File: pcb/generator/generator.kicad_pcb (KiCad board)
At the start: 2 copper layers, 77.5 x 104.5 mm, 53 parts, among them J1 Power, J2 SWD, J3 CH1, J4 CH2, J5 USB, U1 ATSAMD11D14A-SS, U2 SRH05S3V3, U3 L6206D, U4 MCP9700T-HLT, U5 LP2985-3.3, U6 SN65220, Y1 32.768kHz

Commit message: Release preparation
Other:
- board text added: "Meadow Robotics GmbH"
- board text added: "Perimeter Wire Generator R1"
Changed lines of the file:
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@@
   (general
     (thickness 1.6)
-    (drawings 17)
+    (drawings 19)
     (tracks 1861)
     (zones 0)
@@
   )
   (page A4)
+  (title_block
+    (title "Permimeter Wire Generator")
+    (date 2019-09-02)
+    (rev R1)
+    (company "Meadow Robotics GmbH")
+  )
   (layers
     (0 F.Cu signal)
@@
     )
   )
+  (gr_text "Perimeter Wire Generator\nR1" (at 50.8 67.945) (layer F.SilkS)
+    (effects (font (size 1 1) (thickness 0.15)) (justify left))
+  )
+  (gr_text "Meadow Robotics GmbH" (at 50.8 65.405) (layer F.SilkS)
+    (effects (font (size 1 1) (thickness 0.15)) (justify left))
+  )
   (gr_text "USB\n" (at 66.675 58.42) (layer F.SilkS)

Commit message: generator: pcb for modulbox
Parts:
- removed D2: D, Diode_THT:D_DO-35_SOD27_P7.62mm_Horizontal
- removed H1, H2, H3: MountingHole_Pad, MountingHole:MountingHole_3.2mm_M3_Pad
- added C19: 100n, Capacitor_SMD:C_0805_2012Metric, F.Cu at (155.6, 78.1)
- added C9: 100n, Capacitor_SMD:C_0805_2012Metric, F.Cu at (156.2, 57.8)
- added D8: 48V, Diode_SMD:D_SMB, F.Cu at (54.0, 87.6)
- added E1: SPARK_GAP, footprints:Spark_Gap_0.4_Pwr, B.Cu at (43.2, 84.7)
- added E2: SPARK_GAP, footprints:Spark_Gap_0.4_Pwr, B.Cu at (40.6, 47.0)
- added E3: SPARK_GAP, footprints:Spark_Gap_0.4_Pwr, B.Cu at (40.6, 52.1)
- added E4: SPARK_GAP, footprints:Spark_Gap_0.4_Pwr, B.Cu at (40.6, 57.1)
- added E5: SPARK_GAP, footprints:Spark_Gap_0.4_Pwr, B.Cu at (40.6, 62.2)
- added E6: SPARK_GAP, footprints:Spark_Gap_0.4_Pwr, B.Cu at (40.6, 67.3)
- added E7: SPARK_GAP, footprints:Spark_Gap_0.4_Pwr, B.Cu at (40.6, 71.8)
- added FID3: Fiducial, Fiducial:Fiducial_1mm_Mask2mm, F.Cu at (160.0, 84.5)
- added FID4: Fiducial, Fiducial:Fiducial_1mm_Mask2mm, F.Cu at (141.6, 62.2)
- added FID5: Fiducial, Fiducial:Fiducial_1mm_Mask2mm, F.Cu at (130.2, 45.7)
- added FID6: Fiducial, Fiducial:Fiducial_1mm_Mask2mm, F.Cu at (84.5, 54.0)
- added J6: Au, Connector_PinSocket_2.54mm:PinSocket_2x05_P2.54mm_Vertical, B.Cu at (147.2, 47.6)
- added J7: Bu, Connector_PinSocket_2.54mm:PinSocket_2x05_P2.54mm_Vertical, B.Cu at (157.3, 86.4)
- added J8: Al, Connector_PinHeader_2.54mm:PinHeader_2x05_P2.54mm_Vertical, F.Cu at (80.6, 47.6)
- added J9: Bl, Connector_PinHeader_2.54mm:PinHeader_2x05_P2.54mm_Vertical, F.Cu at (90.8, 85.7)
- added R11: 280R, Resistor_SMD:R_0805_2012Metric, F.Cu at (138.4, 53.3)
- added R12: 280R, Resistor_SMD:R_0805_2012Metric, F.Cu at (138.4, 61.0)
- added R13: 100R, Resistor_SMD:R_0805_2012Metric, F.Cu at (138.4, 48.3)
- added R14: 100R, Resistor_SMD:R_0805_2012Metric, F.Cu at (138.4, 50.8)
- added R15: 100R, Resistor_SMD:R_0805_2012Metric, F.Cu at (138.4, 58.4)
- added R16: 100R, Resistor_SMD:R_0805_2012Metric, F.Cu at (138.4, 55.9)
- added R17: 100R, Resistor_SMD:R_0805_2012Metric, F.Cu at (109.2, 46.4)
- C10, C11, C12, C13, C8: footprint Capacitor_THT:C_Disc_D5.1mm_W3.2mm_P5.00mm -> Capacitor_SMD:C_0805_2012Metric
- C14, C15: value 20p -> 22p; footprint Capacitor_THT:C_Disc_D3.8mm_W2.6mm_P2.50mm -> Capacitor_SMD:C_0805_2012Metric
- C16, C17, C3, C4, C5, C6, C7: footprint Capacitor_THT:C_Disc_D4.7mm_W2.5mm_P5.00mm -> Capacitor_SMD:C_0805_2012Metric
- C18: footprint Capacitor_THT:CP_Radial_D5.0mm_P2.00mm -> Capacitor_Tantalum_SMD:CP_EIA-6032-28_Kemet-C
- D1: footprint Diode_THT:D_DO-35_SOD27_P7.62mm_Horizontal -> Package_TO_SOT_SMD:SOT-23
- D3: value Red1 -> CLMVC-FKA; footprint LED_THT:LED_D5.0mm -> LED_SMD:LED_Cree-PLCC4_2x2mm_CW
- D4: value Red2 -> CLMVC-FKA; footprint LED_THT:LED_D5.0mm -> LED_SMD:LED_Cree-PLCC4_2x2mm_CW
- D5: footprint Diode_THT:D_DO-15_P10.16mm_Horizontal -> Diode_SMD:D_SMB
- FB1: value BLM31KN471SN1L -> BLM31KN471SN1L
- FB2: value BLM31SN500SN1 -> BLM31SN500SN1L
- FID1, FID2: footprint Fiducial:Fiducial_1.5mm_Mask3mm -> Fiducial:Fiducial_1mm_Mask2mm
- J1: footprint Connector_Phoenix_MSTB:PhoenixContact_MSTBA_2,5_2-G_1x02_P5.00mm_Horizontal -> TerminalBlock:TerminalBlock_bornier-2_P5.08mm
- J2: footprint Connector_PinHeader_1.27mm:PinHeader_2x05_P1.27mm_Vertical -> Connector_PinHeader_1.27mm:PinHeader_2x05_P1.27mm_Vertical_SMD
- J3, J4: footprint Connector_Phoenix_MSTB:PhoenixContact_MSTBA_2,5_3-G-5,08_1x03_P5.08mm_Horizontal -> TerminalBlock:TerminalBlock_bornier-3_P5.08mm
- J5: footprint Connector_USB:USB_Micro-B_Amphenol_10103594-0001LF_Horizontal -> Connector_USB:USB_Micro-B_Molex-105133-0001
- R1, R2: value 10k -> 22k; footprint Resistor_THT:R_Axial_DIN0207_L6.3mm_D2.5mm_P7.62mm_Horizontal -> Resistor_SMD:R_0805_2012Metric
- R10, R4, R5: footprint Resistor_THT:R_Axial_DIN0207_L6.3mm_D2.5mm_P7.62mm_Horizontal -> Resistor_SMD:R_0805_2012Metric
- R3: value 100 -> 22k; footprint Resistor_THT:R_Axial_DIN0207_L6.3mm_D2.5mm_P7.62mm_Horizontal -> Resistor_SMD:R_0805_2012Metric
- R6, R7: value 240 -> 200R; footprint Resistor_THT:R_Axial_Power_L48.0mm_W12.5mm_P60.96mm -> footprints:Ohmite-TKH
- R8: value 750R -> 1k; footprint Resistor_THT:R_Axial_DIN0207_L6.3mm_D2.5mm_P7.62mm_Horizontal -> Resistor_SMD:R_0805_2012Metric
- R9: value 750R -> 1M; footprint Resistor_THT:R_Axial_DIN0207_L6.3mm_D2.5mm_P7.62mm_Horizontal -> Resistor_SMD:R_0805_2012Metric
- U1: value ATSAMD11D14A-SS -> ATSAMD21E; footprint Package_SO:SOIC-20W_7.5x12.8mm_P1.27mm -> Package_QFP:TQFP-32_7x7mm_P0.8mm
- U3: value L6206D -> L6206
- Y1: value 32.768kHz -> 16MHz; footprint Crystal:Crystal_SMD_SeikoEpson_MC146-4Pin_6.7x1.5mm_HandSoldering -> Crystal:Crystal_SMD_SeikoEpson_TSX3225-4Pin_3.2x2.5mm
- moved J1 104.4 mm to (43.2, 82.2), turned to 270 degrees
- moved R1 100.2 mm to (155.6, 54.0), turned to 270 degrees
- moved R2 100.1 mm to (155.6, 80.6), turned to 0 degrees
- moved FB2 85.4 mm to (57.9, 87.4), turned to 90 degrees
- moved R3 79.9 mm to (164.5, 64.8), turned to 0 degrees
- moved C12 78.6 mm to (60.3, 87.6)
- moved J4 76.4 mm to (43.2, 61.9)
- moved C17 75.7 mm to (130.2, 60.3)
- moved C8 75.5 mm to (117.3, 46.4)
- moved C11 74.6 mm to (97.2, 75.6), turned to 180 degrees
- moved R5 74.5 mm to (90.2, 78.1)
- moved C1 74.3 mm to (96.5, 47.6), turned to 0 degrees
- moved C3 72.1 mm to (153.7, 70.5), turned to 0 degrees
- moved J3 71.7 mm to (43.2, 46.6)
- moved J5 71.1 mm to (135.9, 66.7), turned to 270 degrees
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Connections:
- D1 pad 1: Net-(D1-Pad1) -> +48V
- D1 pad 2: +48V -> Net-(C8-Pad1)
- D3 pad 1: Net-(D3-Pad1) -> +3V3
- D3 pad 2: +3V3 -> Net-(D3-Pad2)
- D4 pad 1: Net-(D4-Pad1) -> +3V3
- D4 pad 2: +3V3 -> Net-(D4-Pad2)
- J3 pad 2: Net-(J3-Pad2) -> Net-(E3-Pad1)
- J3 pad 3: Net-(J3-Pad3) -> Net-(E4-Pad1)
- J4 pad 2: Net-(J4-Pad2) -> Net-(E6-Pad1)
- J4 pad 3: Net-(J4-Pad3) -> Net-(E7-Pad1)
- R3 pad 1: Net-(C16-Pad2) -> /V_SENSE
- R3 pad 2: Net-(D1-Pad1) -> GND
- R6 pad 1: Net-(J3-Pad3) -> Net-(E3-Pad1)
- R6 pad 2: Net-(J3-Pad2) -> GND
- R7 pad 1: Net-(J4-Pad3) -> Net-(E6-Pad1)
- R7 pad 2: Net-(J4-Pad2) -> GND
- R8 pad 1: Net-(D3-Pad1) -> +3V3
- R8 pad 2: Net-(R8-Pad2) -> /SWCLK
- R9 pad 1: Net-(D4-Pad1) -> +48V
- R9 pad 2: Net-(R9-Pad2) -> /V_SENSE
- U1 pad 1: /IN2_B -> /EN_B
- U1 pad 10: Net-(R9-Pad2) -> GND
- U1 pad 11: /~RESET -> /EN_A
- U1 pad 12: /SWCLK -> /ERROR_A
- U1 pad 13: /SWDIO -> (no net)
- U1 pad 14: /USB_D- -> (no net)
- U1 pad 15: /USB_D+ -> Net-(C14-Pad1)
- U1 pad 16: GND -> Net-(C15-Pad2)
- U1 pad 17: +3V3 -> Net-(R13-Pad2)
- U1 pad 18: /EN_B -> Net-(R14-Pad2)
- U1 pad 19: /ERROR_B -> Net-(R11-Pad2)
- U1 pad 2: /IN1_A -> /ERROR_B
- U1 pad 20: /IN1_B -> Net-(R16-Pad2)
- U1 pad 3: /IN2_A -> /IN1_B
- U1 pad 4: Net-(C14-Pad1) -> /IN2_B
- U1 pad 5: Net-(C15-Pad2) -> /V_SENSE
- U1 pad 6: /EN_A -> /R_TEMP
- U1 pad 7: /ERROR_A -> /IN1_A
- U1 pad 8: /R_TEMP -> /IN2_A
- U1 pad 9: Net-(R8-Pad2) -> +3V3
- U3 pad 15: Net-(J3-Pad2) -> Net-(E3-Pad1)
- U3 pad 22: Net-(J4-Pad2) -> Net-(E6-Pad1)
- Y1 pad 3: GND -> Net-(C15-Pad2)
- Y1 pad 4: Net-(C15-Pad2) -> GND
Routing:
- net GND: track 641.8 -> 162.0 mm, vias 1102 -> 434
- net /EN_B: track 170.1 -> 15.8 mm
- net /ERROR_B: track 186.5 -> 59.4 mm, vias 2 -> 1
- net /IN1_B: track 167.1 -> 43.3 mm, vias 4 -> 1
- net /IN2_B: track 152.7 -> 41.7 mm, vias 4 -> 1
- net Net-(J3-Pad3): track 110.0 -> 0.00 mm, vias 2 -> 0
- net Net-(J4-Pad3): track 108.4 -> 0.00 mm
- net /EN_A: track 101.1 -> 5.53 mm, vias 2 -> 0
- net /ERROR_A: track 120.1 -> 37.8 mm, vias 4 -> 2
- net Net-(J4-Pad2): track 80.6 -> 0.00 mm
- net Net-(J3-Pad2): track 78.6 -> 0.00 mm
- net /IN1_A: track 108.2 -> 37.2 mm, vias 4 -> 1
- net +48V: track 151.8 -> 222.7 mm, vias 1 -> 0
- net (no net): track 70.3 -> 0.00 mm, vias 4 -> 0
- net /IN2_A: track 107.6 -> 37.7 mm, vias 4 -> 1
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- added copper zone on F.Cu, net +3V3
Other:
- board size 77.5 x 104.5 mm -> 131 x 50.2 mm
- net class Default: clearance 0.2 -> 0.19
- rule trace_clearance: 0.2 -> 0.19
- board text added: "Meadow Robotics GmbH Perimeter Wire Generator R2"
- board text removed: "Meadow Robotics GmbH"
- board text removed: "Perimeter Wire Generator R1"
- board text removed: "USB"

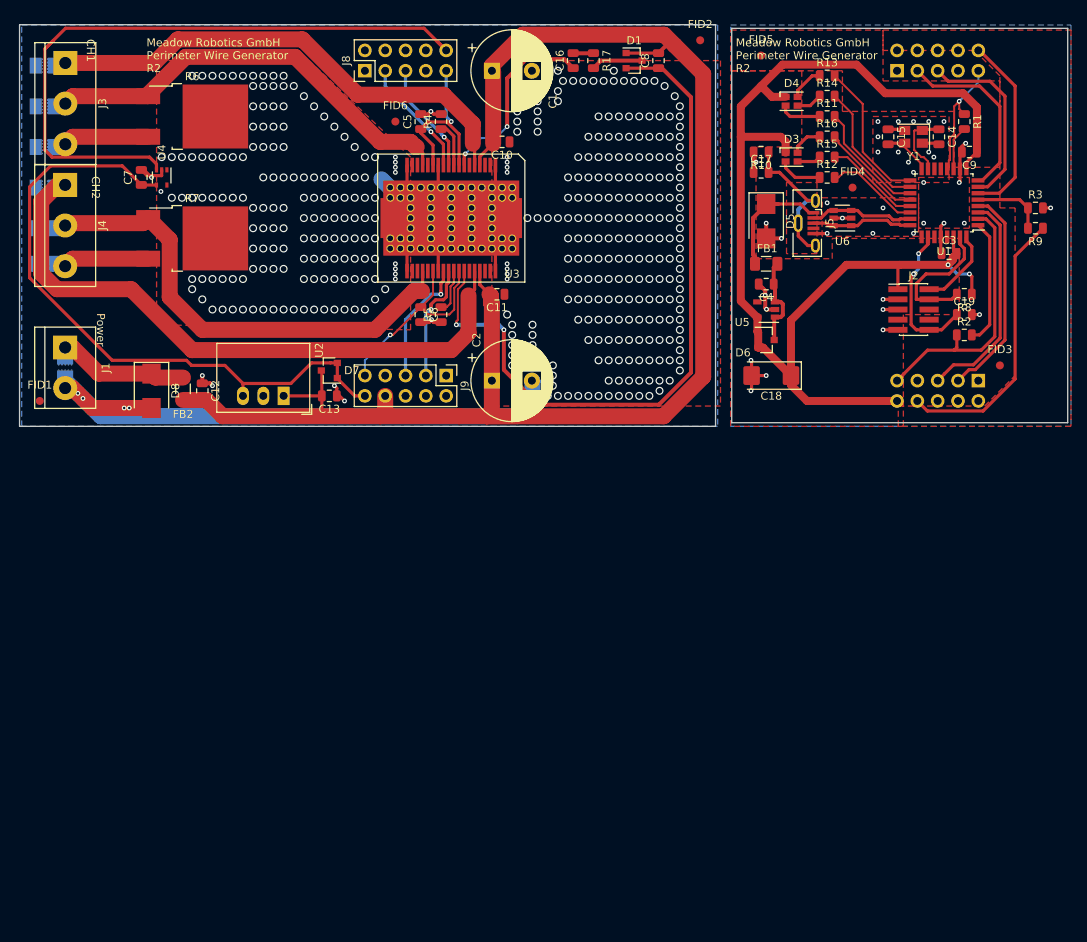
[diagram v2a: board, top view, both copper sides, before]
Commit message: gernerator pcb r2 - place references - adjust mask clearance
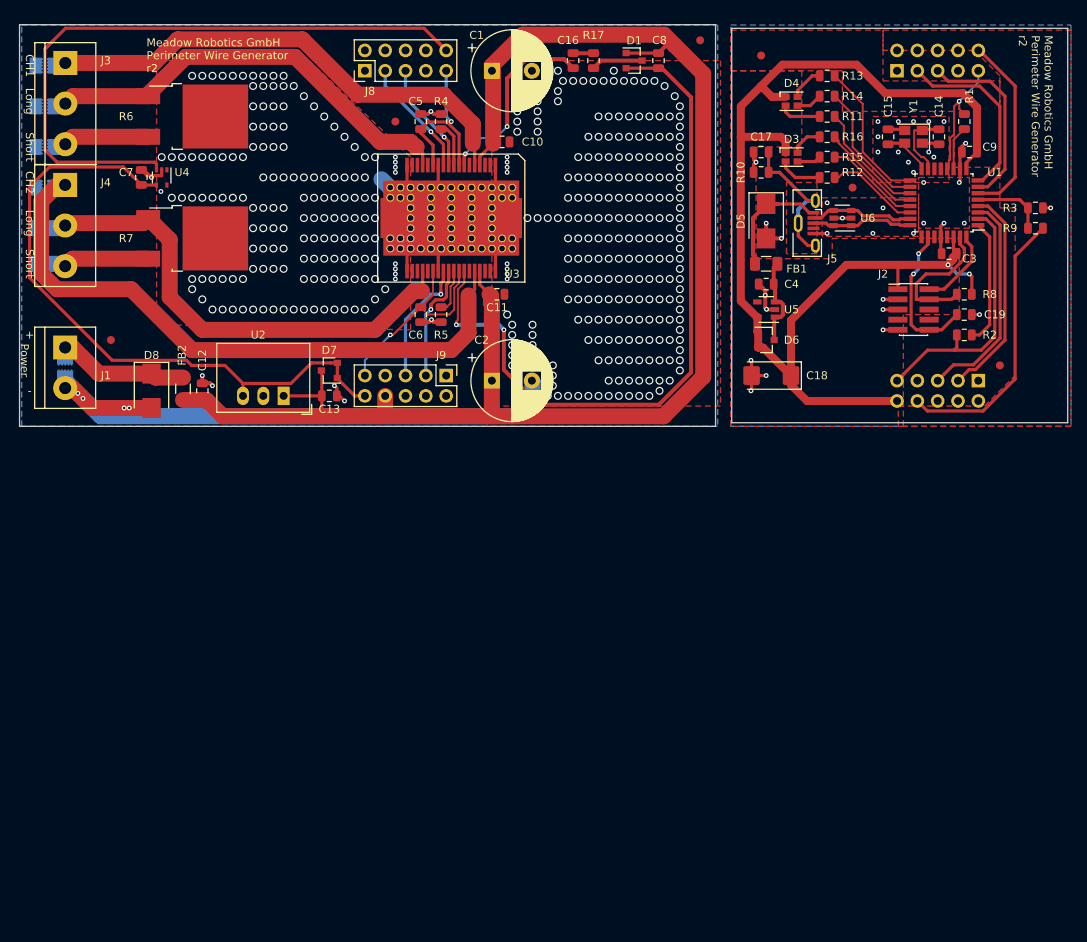
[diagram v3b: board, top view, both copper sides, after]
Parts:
- moved FID1 11.7 mm to (48.9, 81.3)
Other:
- rule pad_to_mask_clearance: 0 -> 0.15
- rule solder_mask_min_width: 0.25 -> 0.05
- board text added: "+"
- board text added: "-"
- board text added: "Connectors on back of pcb!"
- board text added: "Long"
- board text added: "Meadow Robotics GmbH Perimeter Wire Generator r2"
- board text added: "Short"
- board text removed: "Meadow Robotics GmbH Perimeter Wire Generator R2"
